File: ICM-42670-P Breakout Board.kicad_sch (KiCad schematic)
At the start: 11 parts, among them J1 Breakout Header Pins, U1 ICM-42688-P, U2 MCP1700x-330xxTT

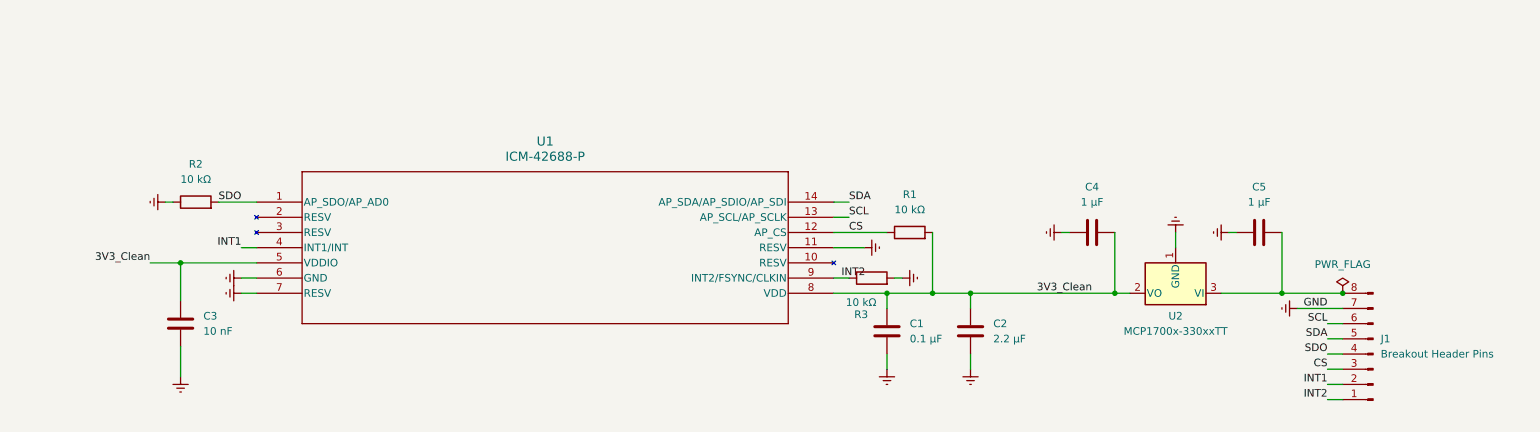
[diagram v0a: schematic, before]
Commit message: Swaped 42688 Sensor for 42670 added Conn_01x9
Swaped 42688 Sensor for 42670 added Conn_01x9

conn_01x9 Includes footprint
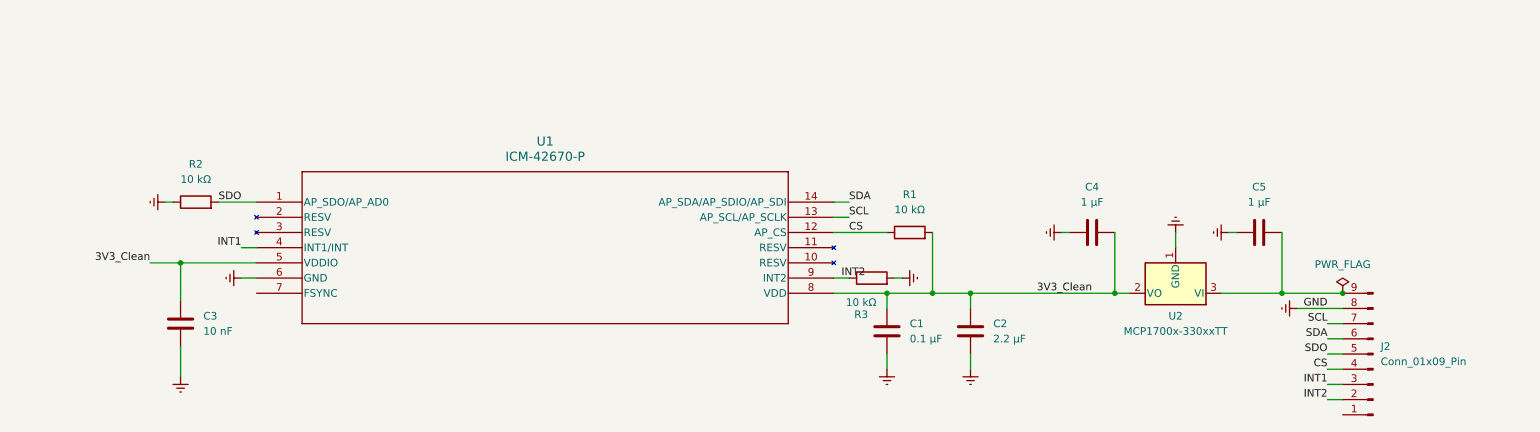
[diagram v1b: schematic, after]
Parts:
- removed J1: Breakout Header Pins, symbol Connector:Conn_01x08_Pin
- removed U1: ICM-42688-P, LGA14_2P5X3X0P91_TDK, symbol 2026-03-06_23-32-59:ICM-42688-P
- added J2: Conn_01x09_Pin, Connector_PinHeader_2.54mm:PinHeader_1x09_P2.54mm_Vertical, symbol Connector:Conn_01x09_Pin
- added U1: ICM-42670-P, LGA14_2.5X3X0.76_IVS, symbol ICM-42670-P:ICM-42670-P
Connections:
- net 3V3_Clean: now also U1.5 (VDDIO), U1.8 (VDD)
- net CS: now also J2.4 (Pin_4), U1.12 (AP_CS)
- net GND: now also J2.8 (Pin_8), U1.6 (GND)
- net INT1: now also J2.3 (Pin_3), U1.4 (INT1/INT)
- net INT2: now also J2.2 (Pin_2), U1.9 (INT2)
- net SCL: now also J2.7 (Pin_7), U1.13 (AP_SCL/AP_SCLK)
- net SDA: now also J2.6 (Pin_6), U1.14 (AP_SDA/AP_SDIO/AP_SDI)
- net SDO: now also J2.5 (Pin_5), U1.1 (AP_SDO/AP_AD0)
- net at C5.2, U2.3 (VI): now also J2.9 (Pin_9)
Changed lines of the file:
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@@
 	(paper "A4")
+	(junction
+		(at 241.3 101.6)
+		(diameter 0)
+		(color 0 0 0 0)
+	)
 	(junction
 		(at 165.1 101.6)
@@
 	)
 	(junction
-		(at 241.3 101.6)
-		(diameter 0)
-		(color 0 0 0 0)
-	)
-	(junction
 		(at 46.99 96.52)
 		(diameter 0)
@@
 	(wire
 		(pts
-			(xy 57.15 101.6) (xy 59.69 101.6)
-		)
-		(stroke
-			(width 0)
-			(type default)
-		)
-	)
-	(wire
-		(pts
 			(xy 233.68 104.14) (xy 241.3 104.14)
 		)
@@
 		(pts
 			(xy 44.45 86.36) (xy 45.72 86.36)
-		)
-		(stroke
-			(width 0)
-			(type default)
-		)
-	)
-	(wire
-		(pts
-			(xy 156.21 93.98) (xy 161.29 93.98)
 		)
 		(stroke
@@
 	)
 	(symbol
-		(lib_id "power:Earth")
-		(at 161.29 93.98 90)
+		(lib_id "Connector:Conn_01x09_Pin")
+		(at 246.38 111.76 180)
 		(unit 1)
 		(exclude_from_sim no)
@@
 		(dnp no)
 		(fields_autoplaced yes)
-		(property "Reference" "#PWR013"
-			(at 167.64 93.98 0)
-			(effects
-				(font
-					(size 1.27 1.27)
-				)
-				(hide yes)
-			)
-		)
-		(property "Value" "GND"
-			(at 165.1 93.9799 90)
+		(property "Reference" "J2"
+			(at 247.65 110.4899 0)
 			(effects
 				(font
@@
 				)
 				(justify right)
-				(hide yes)
-			)
-		)
-		(property "Footprint" ""
-			(at 161.29 93.98 0)
+			)
+		)
+		(property "Value" "Conn_01x09_Pin"
+			(at 247.65 113.0299 0)
+			(effects
+				(font
+					(size 1.27 1.27)
+				)
+				(justify right)
+			)
+		)
+		(property "Footprint" "Connector_PinHeader_2.54mm:PinHeader_1x09_P2.54mm_Vertical"
+			(at 246.38 111.76 0)
 			(effects
 				(font
@@
 		)
 		(property "Datasheet" "~"
-			(at 161.29 93.98 0)
-			(effects
-				(font
-					(size 1.27 1.27)
-				)
-				(hide yes)
-			)
-		)
-		(property "Description" "Power symbol creates a global label with name \"Earth\""
-			(at 161.29 93.98 0)
-			(effects
-				(font
-					(size 1.27 1.27)
-				)
-				(hide yes)
-			)
+			(at 246.38 111.76 0)
+			(effects
+				(font
+					(size 1.27 1.27)
+				)
+				(hide yes)
+			)
+		)
+		(property "Description" "Generic connector, single row, 01x09, script generated"
+			(at 246.38 111.76 0)
+			(effects
+				(font
+					(size 1.27 1.27)
+				)
+				(hide yes)
+			)
+		)
+		(pin "3"
+		)
+		(pin "6"
+		)
+		(pin "5"
+		)
+		(pin "7"
+		)
+		(pin "9"
+		)
+		(pin "4"
 		)
 		(pin "1"
+		)
+		(pin "8"
+		)
+		(pin "2"
 		)
 		(instances
 			(project ""
 				(path "/46f757aa-f0ff-4bf0-8e74-16936fa9d7c2"
-					(reference "#PWR013")
+					(reference "J2")
 					(unit 1)
 				)
@@
 	(symbol
 		(lib_id "power:Earth")
-		(at 57.15 101.6 270)
-		(unit 1)
-		(exclude_from_sim no)
-		(in_bom yes)
-		(on_board yes)
-		(dnp no)
-		(fields_autoplaced yes)
-		(property "Reference" "#PWR05"
-			(at 50.8 101.6 0)
-			(effects
-				(font
-					(size 1.27 1.27)
-				)
-				(hide yes)
-			)
-		)
-		(property "Value" "GND"
-			(at 53.34 101.5999 90)
-			(effects
-				(font
-					(size 1.27 1.27)
-				)
-				(justify right)
-				(hide yes)
-			)
-		)
-		(property "Footprint" ""
-			(at 57.15 101.6 0)
-			(effects
-				(font
-					(size 1.27 1.27)
-				)
-				(hide yes)
-			)
-		)
-		(property "Datasheet" "~"
-			(at 57.15 101.6 0)
-			(effects
-				(font
-					(size 1.27 1.27)
-				)
-				(hide yes)
-			)
-		)
-		(property "Description" "Power symbol creates a global label with name \"Earth\""
-			(at 57.15 101.6 0)
-			(effects
-				(font
-					(size 1.27 1.27)
-				)
-				(hide yes)
-			)
-		)
-		(pin "1"
-		)
-		(instances
-			(project "ICM-42688-P Breakout Board"
-				(path "/46f757aa-f0ff-4bf0-8e74-16936fa9d7c2"
-					(reference "#PWR05")
-					(unit 1)
-				)
-			)
-		)
-	)
-	(symbol
-		(lib_id "power:Earth")
 		(at 46.99 115.57 0)
 		(unit 1)
@@
 	)
 	(symbol
-		(lib_id "2026-03-06_23-32-59:ICM-42688-P")
-		(at 59.69 86.36 0)
-		(unit 1)
-		(exclude_from_sim no)
-		(in_bom yes)
-		(on_board yes)
-		(dnp no)
-		(fields_autoplaced yes)
-		(property "Reference" "U1"
-			(at 107.95 76.2 0)
-			(effects
-				(font
-					(size 1.524 1.524)
-				)
-			)
-		)
-		(property "Value" "ICM-42688-P"
-			(at 107.95 78.74 0)
-			(effects
-				(font
-					(size 1.524 1.524)
-				)
-			)
-		)
-		(property "Footprint" "LGA14_2P5X3X0P91_TDK"
-			(at 59.69 86.36 0)
-			(effects
-				(font
-					(size 1.27 1.27)
-					(italic yes)
-				)
-				(hide yes)
-			)
-		)
-		(property "Datasheet" "ICM-42688-P"
-			(at 59.69 86.36 0)
-			(effects
-				(font
-					(size 1.27 1.27)
-					(italic yes)
-				)
-				(hide yes)
-			)
-		)
-		(property "Description" ""
-			(at 59.69 86.36 0)
-			(effects
-				(font
-					(size 1.27 1.27)
-				)
-				(hide yes)
-			)
-		)
-		(pin "12"
-		)
-		(pin "9"
-		)
-		(pin "1"
-		)
-		(pin "7"
-		)
-		(pin "5"
-		)
-		(pin "3"
-		)
-		(pin "4"
-		)
-		(pin "2"
-		)
-		(pin "6"
-		)
-		(pin "14"
-		)
-		(pin "13"
-		)
-		(pin "11"
-		)
-		(pin "10"
-		)
-		(pin "8"
-		)
-		(instances
-			(project ""
-				(path "/46f757aa-f0ff-4bf0-8e74-16936fa9d7c2"
-					(reference "U1")
-					(unit 1)
-				)
-			)
-		)
-	)
-	(symbol
 		(lib_id "power:Earth")
 		(at 44.45 86.36 270)
@@
 	)
 	(symbol
-		(lib_id "Connector:Conn_01x08_Pin")
-		(at 246.38 111.76 180)
+		(lib_id "ICM-42670-P:ICM-42670-P")
+		(at 59.69 86.36 0)
 		(unit 1)
 		(exclude_from_sim no)
@@
 		(dnp no)
 		(fields_autoplaced yes)
-		(property "Reference" "J1"
-			(at 247.65 109.2199 0)
-			(effects
-				(font
-					(size 1.27 1.27)
-				)
-				(justify right)
-			)
-		)
-		(property "Value" "Breakout Header Pins"
-			(at 247.65 111.7599 0)
-			(effects
-				(font
-					(size 1.27 1.27)
-				)
-				(justify right)
-			)
-		)
-		(property "Footprint" ""
-			(at 246.38 111.76 0)
-			(effects
-				(font
-					(size 1.27 1.27)
-				)
-				(hide yes)
-			)
-		)
-		(property "Datasheet" "~"
-			(at 246.38 111.76 0)
-			(effects
-				(font
-					(size 1.27 1.27)
-				)
-				(hide yes)
-			)
-		)
-		(property "Description" "Generic connector, single row, 01x08, script generated"
-			(at 246.38 111.76 0)
-			(effects
-				(font
-					(size 1.27 1.27)
-				)
-				(hide yes)
-			)
+		(property "Reference" "U1"
+			(at 107.95 76.2 0)
+			(effects
+				(font
+					(size 1.524 1.524)
+				)
+			)
+		)
+		(property "Value" "ICM-42670-P"
+			(at 107.95 78.74 0)
+			(effects
+				(font
+					(size 1.524 1.524)
+				)
+			)
+		)
+		(property "Footprint" "LGA14_2.5X3X0.76_IVS"
+			(at 59.69 86.36 0)
+			(effects
+				(font
+					(size 1.27 1.27)
+					(italic yes)
+				)
+				(hide yes)
+			)
+		)
+		(property "Datasheet" "ICM-42670-P"
+			(at 59.69 86.36 0)
+			(effects
+				(font
+					(size 1.27 1.27)
+					(italic yes)
+				)
+				(hide yes)
+			)
+		)
+		(property "Description" ""
+			(at 59.69 86.36 0)
+			(effects
+				(font
+					(size 1.27 1.27)
+				)
+				(hide yes)
+			)
+		)
+		(pin "1"
+		)
+		(pin "7"
+		)
+		(pin "5"
+		)
+		(pin "4"
+		)
+		(pin "12"
+		)
+		(pin "11"
+		)
+		(pin "9"
+		)
+		(pin "13"
+		)
+		(pin "10"
+		)
+		(pin "8"
 		)
 		(pin "3"
 		)
-		(pin "8"
-		)
-		(pin "5"
-		)
 		(pin "6"
 		)
-		(pin "1"
+		(pin "14"
 		)
 		(pin "2"
-		)
-		(pin "4"
-		)
-		(pin "7"
 		)
 		(instances
 			(project ""
 				(path "/46f757aa-f0ff-4bf0-8e74-16936fa9d7c2"
-					(reference "J1")
+					(reference "U1")
 					(unit 1)
 				)

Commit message: Wired FSYNC with Pull down ground
Wired FSYNC with Pull down ground
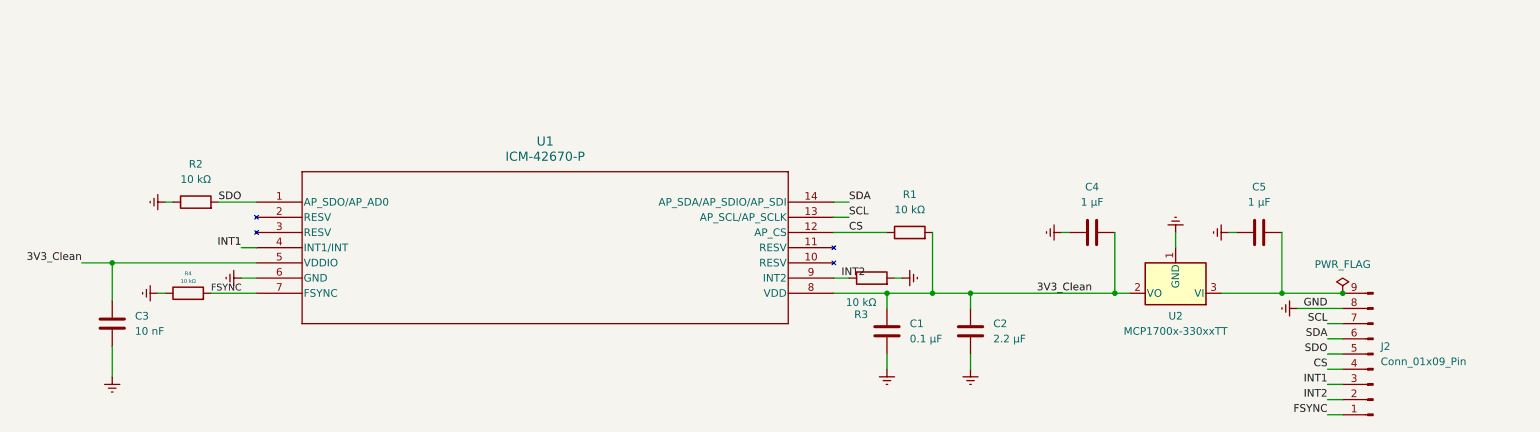
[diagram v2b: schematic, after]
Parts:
- added R4: 10 kΩ, symbol Device:R
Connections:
- net GND: now also R4.1
- net FSYNC: now reaches J2.1 (Pin_1)
- net FSYNC: now also U1.7 (FSYNC), R4.2
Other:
- moved on the sheet: C3
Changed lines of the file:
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@@
 	)
 	(junction
-		(at 46.99 96.52)
+		(at 35.56 96.52)
 		(diameter 0)
 		(color 0 0 0 0)
@@
 	(wire
 		(pts
-			(xy 46.99 96.52) (xy 46.99 102.87)
+			(xy 35.56 96.52) (xy 35.56 102.87)
 		)
 		(stroke
@@
 	(wire
 		(pts
-			(xy 41.91 96.52) (xy 46.99 96.52)
+			(xy 30.48 96.52) (xy 35.56 96.52)
+		)
+		(stroke
+			(width 0)
+			(type default)
+		)
+	)
+	(wire
+		(pts
+			(xy 43.18 101.6) (xy 44.45 101.6)
 		)
 		(stroke
@@
 	(wire
 		(pts
+			(xy 238.76 121.92) (xy 241.3 121.92)
+		)
+		(stroke
+			(width 0)
+			(type default)
+		)
+	)
+	(wire
+		(pts
 			(xy 222.25 91.44) (xy 223.52 91.44)
 		)
@@
 	(wire
 		(pts
-			(xy 46.99 110.49) (xy 46.99 115.57)
+			(xy 35.56 110.49) (xy 35.56 115.57)
 		)
 		(stroke
@@
 	(wire
 		(pts
+			(xy 52.07 101.6) (xy 59.69 101.6)
+		)
+		(stroke
+			(width 0)
+			(type default)
+		)
+	)
+	(wire
+		(pts
 			(xy 172.72 91.44) (xy 172.72 101.6)
 		)
@@
 	(wire
 		(pts
-			(xy 46.99 96.52) (xy 59.69 96.52)
+			(xy 35.56 96.52) (xy 59.69 96.52)
 		)
 		(stroke
@@
 		)
 	)
+	(label "FSYNC"
+		(at 52.07 101.6 0)
+		(effects
+			(font
+				(size 1.143 1.143)
+			)
+			(justify left bottom)
+		)
+	)
 	(label "CS"
 		(at 238.76 114.3 180)
@@
 		)
 	)
+	(label "FSYNC"
+		(at 238.76 121.92 180)
+		(effects
+			(font
+				(size 1.27 1.27)
+			)
+			(justify right bottom)
+		)
+	)
 	(label "3V3_Clean"
-		(at 41.91 96.52 180)
+		(at 30.48 96.52 180)
 		(effects
 			(font
@@
 	(symbol
 		(lib_id "power:Earth")
-		(at 46.99 115.57 0)
+		(at 35.56 115.57 0)
 		(unit 1)
 		(exclude_from_sim no)
@@
 		(fields_autoplaced yes)
 		(property "Reference" "#PWR018"
-			(at 46.99 121.92 0)
+			(at 35.56 121.92 0)
 			(effects
 				(font
@@
 		)
 		(property "Value" "GND"
-			(at 46.99 120.65 0)
+			(at 35.56 120.65 0)
 			(effects
 				(font
@@
 		)
 		(property "Footprint" ""
-			(at 46.99 115.57 0)
+			(at 35.56 115.57 0)
 			(effects
 				(font
@@
 		)
 		(property "Datasheet" "~"
-			(at 46.99 115.57 0)
+			(at 35.56 115.57 0)
 			(effects
 				(font
@@
 		)
 		(property "Description" "Power symbol creates a global label with name \"Earth\""
-			(at 46.99 115.57 0)
+			(at 35.56 115.57 0)
 			(effects
 				(font
@@
 	)
 	(symbol
+		(lib_id "power:Earth")
+		(at 43.18 101.6 270)
+		(unit 1)
+		(exclude_from_sim no)
+		(in_bom yes)
+		(on_board yes)
+		(dnp no)
+		(fields_autoplaced yes)
+		(property "Reference" "#PWR05"
+			(at 36.83 101.6 0)
+			(effects
+				(font
+					(size 1.27 1.27)
+				)
+				(hide yes)
+			)
+		)
+		(property "Value" "GND"
+			(at 39.37 101.5999 90)
+			(effects
+				(font
+					(size 1.27 1.27)
+				)
+				(justify right)
+				(hide yes)
+			)
+		)
+		(property "Footprint" ""
+			(at 43.18 101.6 0)
+			(effects
+				(font
+					(size 1.27 1.27)
+				)
+				(hide yes)
+			)
+		)
+		(property "Datasheet" "~"
+			(at 43.18 101.6 0)
+			(effects
+				(font
+					(size 1.27 1.27)
+				)
+				(hide yes)
+			)
+		)
+		(property "Description" "Power symbol creates a global label with name \"Earth\""
+			(at 43.18 101.6 0)
+			(effects
+				(font
+					(size 1.27 1.27)
+				)
+				(hide yes)
+			)
+		)
+		(pin "1"
+		)
+		(instances
+			(project "ICM-42670-P Breakout Board"
+				(path "/46f757aa-f0ff-4bf0-8e74-16936fa9d7c2"
+					(reference "#PWR05")
+					(unit 1)
+				)
+			)
+		)
+	)
+	(symbol
 		(lib_id "Device:C")
 		(at 227.33 91.44 90)
@@
 	)
 	(symbol
+		(lib_id "Device:R")
+		(at 48.26 101.6 90)
+		(unit 1)
+		(exclude_from_sim no)
+		(in_bom yes)
+		(on_board yes)
+		(dnp no)
+		(property "Reference" "R4"
+			(at 48.26 98.298 90)
+			(effects
+				(font
+					(size 0.635 0.635)
+				)
+			)
+		)
+		(property "Value" "10 kΩ"
+			(at 48.26 99.568 90)
+			(effects
+				(font
+					(size 0.635 0.635)
+				)
+			)
+		)
+		(property "Footprint" ""
+			(at 48.26 103.378 90)
+			(effects
+				(font
+					(size 1.27 1.27)
+				)
+				(hide yes)
+			)
+		)
+		(property "Datasheet" "~"
+			(at 48.26 101.6 0)
+			(effects
+				(font
+					(size 1.27 1.27)
+				)
+				(hide yes)
+			)
+		)
+		(property "Description" "Resistor"
+			(at 48.26 101.6 0)
+			(effects
+				(font
+					(size 1.27 1.27)
+				)
+				(hide yes)
+			)
+		)
+		(pin "2"
+		)
+		(pin "1"
+		)
+		(instances
+			(project "ICM-42670-P Breakout Board"
+				(path "/46f757aa-f0ff-4bf0-8e74-16936fa9d7c2"
+					(reference "R4")
+					(unit 1)
+				)
+			)
+		)
+	)
+	(symbol
 		(lib_id "Device:C")
-		(at 46.99 106.68 0)
+		(at 35.56 106.68 0)
 		(unit 1)
 		(exclude_from_sim no)
@@
 		(fields_autoplaced yes)
 		(property "Reference" "C3"
-			(at 50.8 105.4099 0)
+			(at 39.37 105.4099 0)
 			(effects
 				(font
@@
 		)
 		(property "Value" "10 nF"
-			(at 50.8 107.9499 0)
+			(at 39.37 107.9499 0)
 			(effects
 				(font
@@
 		)
 		(property "Footprint" ""
-			(at 47.9552 110.49 0)
+			(at 36.5252 110.49 0)
 			(effects
 				(font
@@
 		)
 		(property "Datasheet" "~"
-			(at 46.99 106.68 0)
+			(at 35.56 106.68 0)
 			(effects
 				(font
@@
 		)
 		(property "Description" "Unpolarized capacitor"
-			(at 46.99 106.68 0)
-			(effects
-				(font
+			(at 35.56 106.68 0)
+			(effects
+				(font

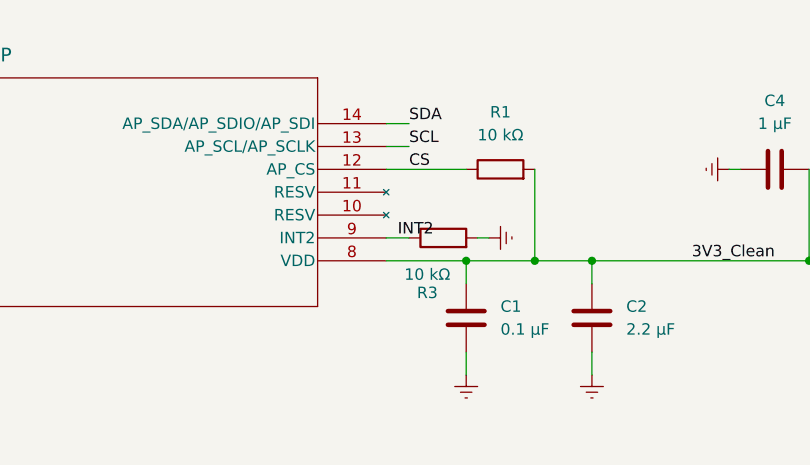
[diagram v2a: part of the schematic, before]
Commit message: Added Missing Footprints
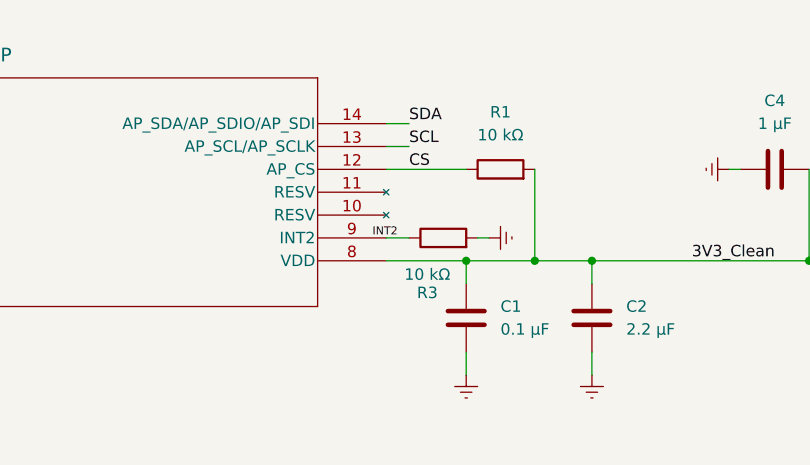
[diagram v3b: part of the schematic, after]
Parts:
- C1, C2, C3, C4, C5: footprint (none) -> Capacitor_SMD:C_0402_1005Metric
- R1, R2, R3, R4: footprint (none) -> Resistor_SMD:R_0402_1005Metric
- U1: footprint LGA14_2.5X3X0.76_IVS -> ICM-42670-P:LGA14_2.5X3X0.76_IVS

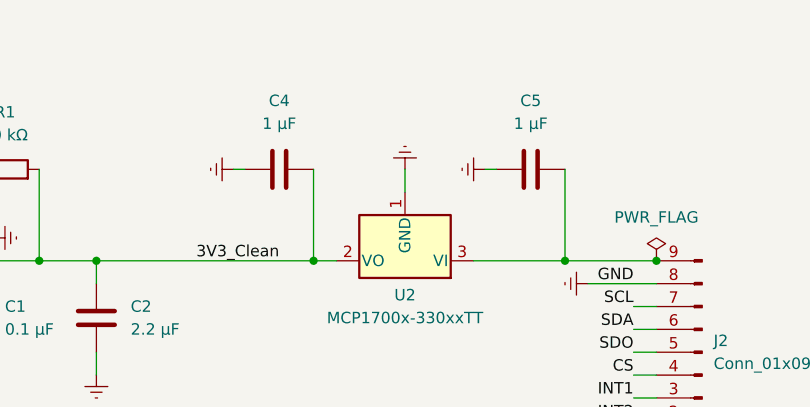
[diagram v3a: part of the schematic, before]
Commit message: Changed Capacitor for Voltage Regulators to 2.2 microFarads for better part selection and reduce part complexity
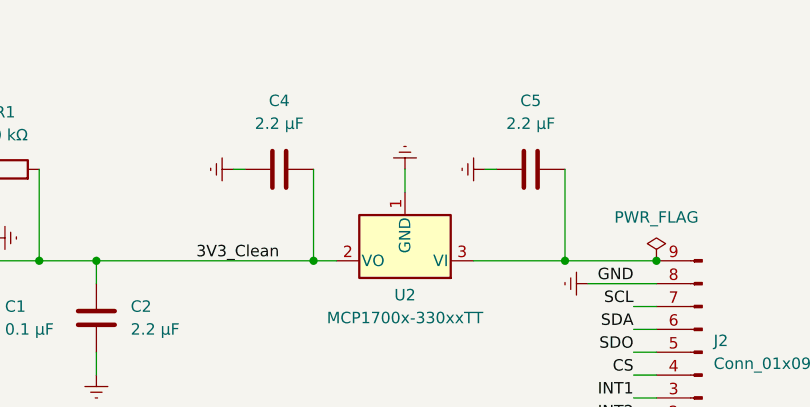
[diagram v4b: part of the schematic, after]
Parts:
- C1: Specification (none) -> X7R, 0.1 µF ±10% >= 16V
- C2: Specification (none) -> X7R, 2.2 µF ±10% 16V
- C4, C5: value 1 µF -> 2.2 µF; Specification (none) -> X7R, 2.2 µF ±10% 16V
